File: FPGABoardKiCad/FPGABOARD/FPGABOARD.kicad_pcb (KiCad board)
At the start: 4 copper layers, 87 parts, among them J1 USB_C_Receptacle_USB2.0_14P, J2 12PMOD, J3 Conn_02x12_Odd_Even, J4 6PMOD, J5 I2C, SW1 ResetICE, SW2 BTN0, SW3 BTN1, SW4 BTN2, U1 ICE40HX1K-VQ100, U2 AP2127K-3.3, U3 W25Q32JVSS, U4 AP2127K-1.2, U5 FT2232HPQ, U6 93LCxxBxxOT, U7 IS62LV256AL, Y2 SG-210STF, Y3 SG-210STF

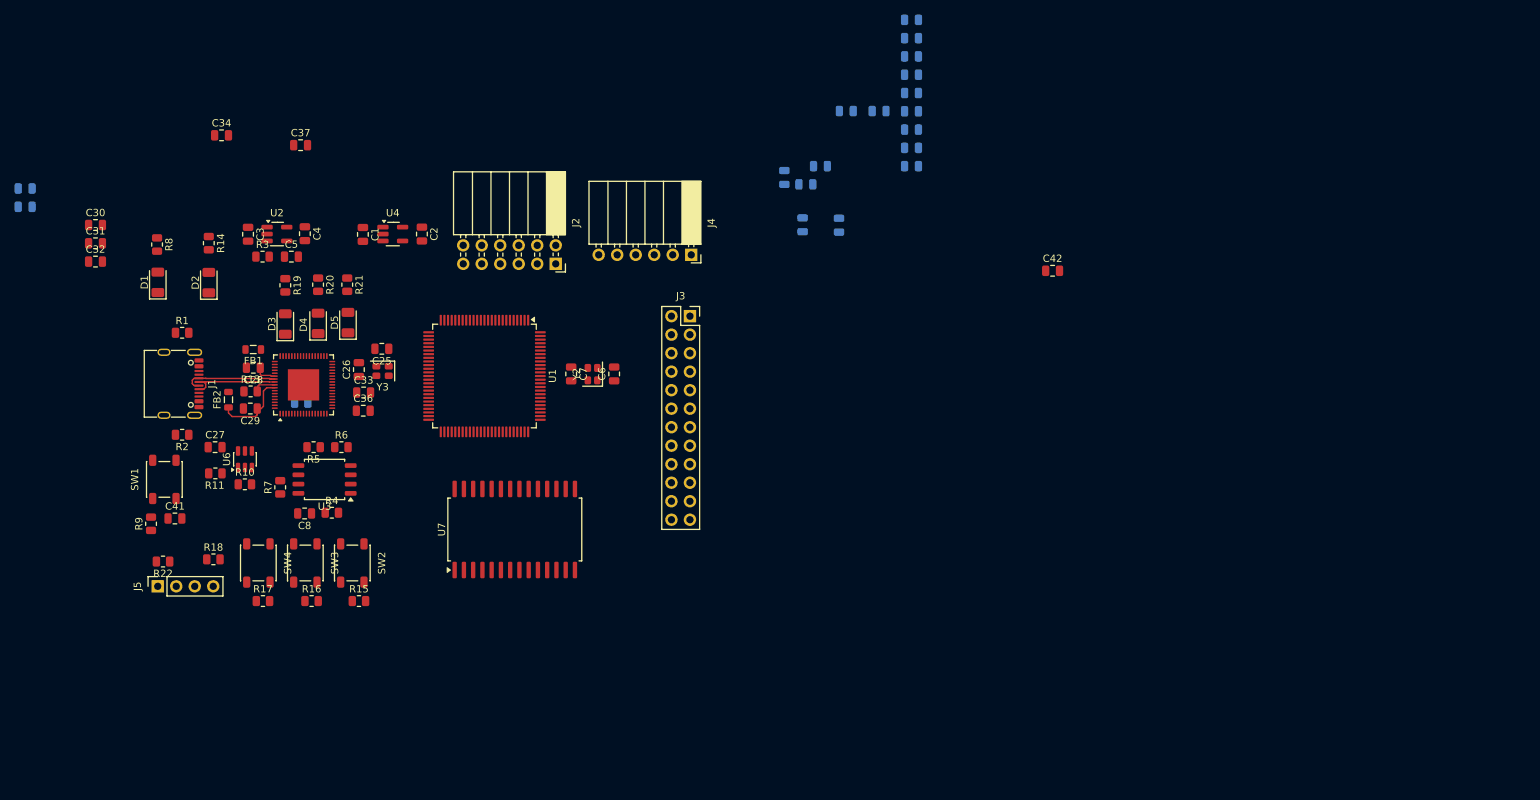
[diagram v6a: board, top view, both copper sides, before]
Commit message: Finsished up Header and Memory routing
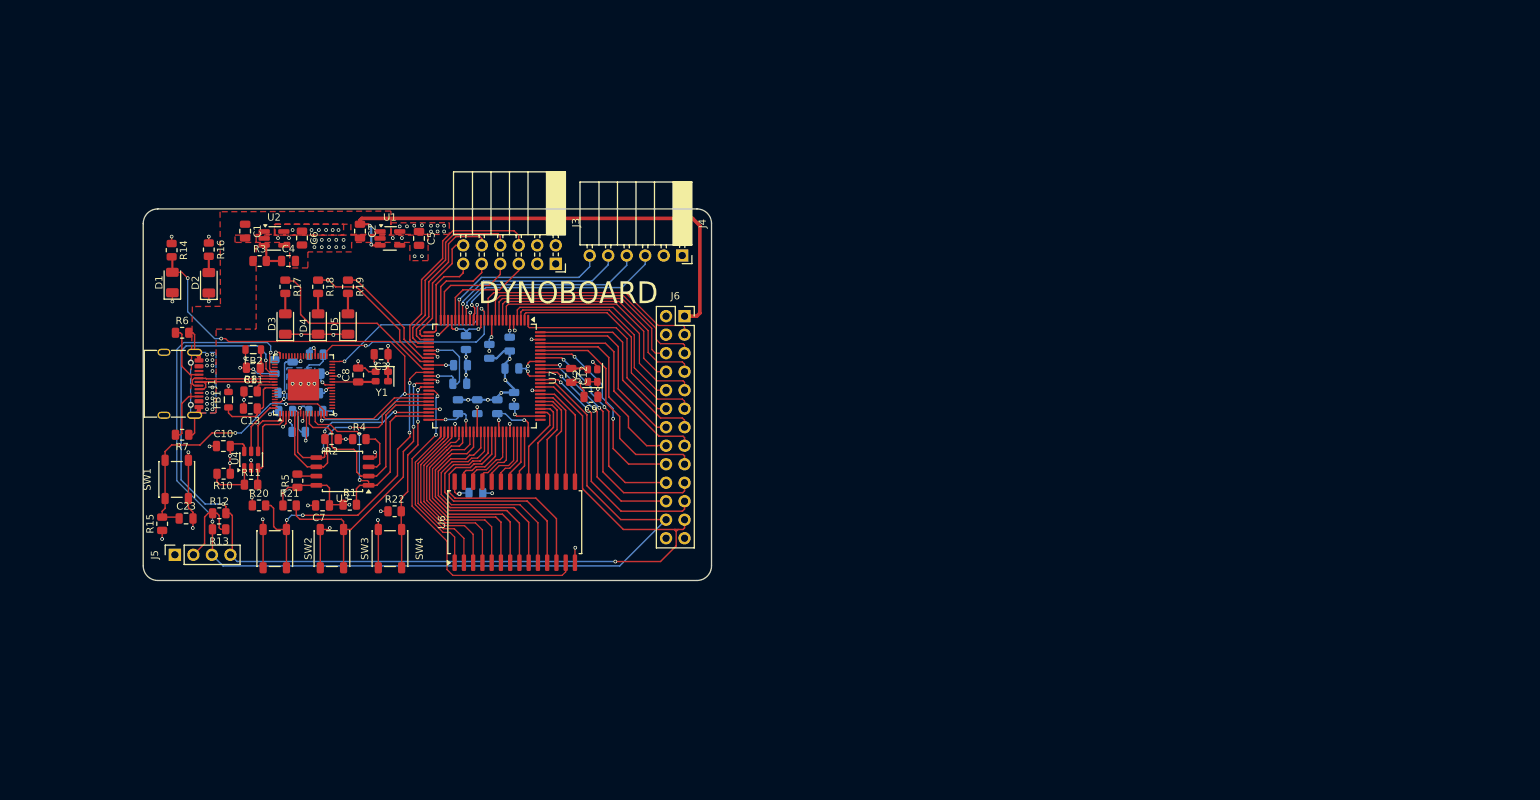
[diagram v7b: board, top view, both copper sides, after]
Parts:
- removed the C10 at (175.5, 78.2)
- removed the C11 at (170.5, 78.2)
- removed the C12 at (172.9, 70.1)
- removed the C13 at (170.9, 72.6)
- removed the C14 at (185.4, 50.0)
- removed the C20 at (185.4, 65.1)
- removed the C23 at (181.0, 62.6)
- removed C37, C38, C39, C42: 100n, Capacitor_SMD:C_0805_2012Metric
- removed the C9 at (168.0, 71.7)
- removed the J3 at (155.0, 90.7)
- added C25: 100n, Capacitor_SMD:C_0805_2012Metric, B.Cu at (123.5, 100.0)
- added C26: 100n, Capacitor_SMD:C_0805_2012Metric, B.Cu at (127.5, 95.5)
- added C27: 100n, Capacitor_SMD:C_0805_2012Metric, B.Cu at (128.6, 103.2)
- added C28: 100n, Capacitor_SMD:C_0805_2012Metric, B.Cu at (125.8, 103.2)
- added C29: 100n, Capacitor_SMD:C_0805_2012Metric, B.Cu at (123.2, 103.2)
- added J6: Conn_02x13_Odd_Even, Connector_PinSocket_2.54mm:PinSocket_2x13_P2.54mm_Vertical, F.Cu at (154.3, 90.7)
- C14: renamed from C36; moved to B.Cu
- C20: renamed from C33; moved to B.Cu
- C24: value 10u -> 100n
- C30, C31, C32, C34: moved to B.Cu
- moved C16 98.7 mm to (99.5, 103.8)
- moved C15 96.3 mm to (100.5, 98.0), turned to -90 degrees
- moved C18 95.2 mm to (98.0, 97.7), turned to -90 degrees
- moved C19 94.3 mm to (99.5, 101.2), turned to 0 degrees
- moved C17 93.9 mm to (103.7, 103.8), turned to 0 degrees
- moved C21 87.7 mm to (103.5, 98.6)
- moved C22 74.8 mm to (125.7, 115.0), turned to 0 degrees
- moved C24 63.4 mm to (123.5, 97.5), turned to 0 degrees
- moved C31 61.3 mm to (130.9, 102.2), turned to 90 degrees
- moved C32 59.0 mm to (130.6, 97.9), turned to 180 degrees
- moved C30 53.3 mm to (124.3, 94.3), turned to -90 degrees
- moved C34 48.8 mm to (130.3, 94.5), turned to -90 degrees
- moved R22 21.9 mm to (114.5, 117.5)
- moved R20 19.0 mm to (95.9, 116.7)
- moved SW4 18.2 mm to (113.9, 122.6)
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- renumbered C3 to C1, C27 to C10, C28 to C11, C7 to C12, C29 to C13, C1 to C2, C41 to C23, C25 to C3, C5 to C4, C2 to C5, C4 to C6, C8 to C7, C26 to C8, C6 to C9, FB2 to FB1, FB1 to FB2, J2 to J3, R4 to R1, R11 to R10, R10 to R11, R18 to R12, R22 to R13, R8 to R14, R9 to R15, R14 to R16, R19 to R17, R20 to R18, R21 to R19, R5 to R2, R15 to R20, R16 to R21, R17 to R22, R6 to R4, R7 to R5, R1 to R6, R2 to R7, R13 to R8, R12 to R9, U4 to U1, U6 to U4, U7 to U6, U1 to U7, Y3 to Y1
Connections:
- C15 pad 1: +3V3 -> +1V2
- C17 pad 1: +3V3 -> +1V2
- C19 pad 1: +3V3 -> +1V2
- C24 pad 1: +3V3 -> +1V2
- C31 pad 1: +3V3 -> +1V2
- U6 pad 1: unconnected-(U7-A14-Pad1) -> /RAMA14
- U6 pad 10: unconnected-(U7-A0-Pad10) -> /RAMA0
- U6 pad 11: unconnected-(U7-I/O0-Pad11) -> /RAMIO0
- U6 pad 12: unconnected-(U7-I/O1-Pad12) -> /RAMIO1
- U6 pad 13: unconnected-(U7-I/O2-Pad13) -> /RAMIO2
- U6 pad 15: unconnected-(U7-I/O3-Pad15) -> /RAMIO3
- U6 pad 16: unconnected-(U7-I/O4-Pad16) -> /RAMIO4
- U6 pad 17: unconnected-(U7-I/O5-Pad17) -> /RAMIO5
- U6 pad 18: unconnected-(U7-I/O6-Pad18) -> /RAMIO6
- U6 pad 19: unconnected-(U7-I/O7-Pad19) -> /RAMIO7
- U6 pad 2: unconnected-(U7-A12-Pad2) -> /RAMA12
- U6 pad 21: unconnected-(U7-A10-Pad21) -> /RAMA10
- U6 pad 23: unconnected-(U7-A11-Pad23) -> /RAMA11
- U6 pad 24: unconnected-(U7-A9-Pad24) -> /RAMA9
- U6 pad 25: unconnected-(U7-A8-Pad25) -> /RAMA8
- U6 pad 26: unconnected-(U7-A13-Pad26) -> /RAMA13
- U6 pad 3: unconnected-(U7-A7-Pad3) -> /RAMA7
- U6 pad 4: unconnected-(U7-A6-Pad4) -> /RAMA6
- U6 pad 5: unconnected-(U7-A5-Pad5) -> /RAMA5
- U6 pad 6: unconnected-(U7-A4-Pad6) -> /RAMA4
- U6 pad 7: unconnected-(U7-A3-Pad7) -> /RAMA3
- U6 pad 8: unconnected-(U7-A2-Pad8) -> /RAMA2
- U6 pad 9: unconnected-(U7-A1-Pad9) -> /RAMA1
- U7 pad 1: unconnected-(U1-IOL_1A-Pad1) -> /EXP13
- U7 pad 10: unconnected-(U1-IOL_5B-Pad10) -> /EXP1
- U7 pad 100: unconnected-(U1-IOT_95-Pad100) -> /EXP5
- U7 pad 12: unconnected-(U1-IOL_6A-Pad12) -> /EXP0
- U7 pad 13: unconnected-(U1-IOL_6B_GBIN7-Pad13) -> /ICETX
- U7 pad 15: unconnected-(U1-IOL_7A_GBIN6-Pad15) -> /ICERX
- U7 pad 16: unconnected-(U1-IOL_7B-Pad16) -> /PMOD3B
- U7 pad 18: unconnected-(U1-IOL_8A-Pad18) -> /PMOD2B
- U7 pad 19: unconnected-(U1-IOL_8B-Pad19) -> /PMOD1B
- U7 pad 2: unconnected-(U1-IOL_1B-Pad2) -> /EXP4
- U7 pad 20: unconnected-(U1-IOL_10A-Pad20) -> /PMOD0B
- U7 pad 21: unconnected-(U1-IOL_10B-Pad21) -> /PMOD7
- U7 pad 24: unconnected-(U1-IOL_12A-Pad24) -> /PMOD6
- U7 pad 25: unconnected-(U1-IOL_12B-Pad25) -> /PMOD5
- U7 pad 26: unconnected-(U1-IOB_26-Pad26) -> /PMOD4
- U7 pad 27: unconnected-(U1-IOB_27-Pad27) -> /PMOD0
- U7 pad 28: unconnected-(U1-IOB_28-Pad28) -> /PMOD1
- U7 pad 29: unconnected-(U1-IOB_29-Pad29) -> /PMOD2
- U7 pad 3: unconnected-(U1-IOL_2A-Pad3) -> /EXP12
- U7 pad 30: unconnected-(U1-IOB_30-Pad30) -> /PMOD3
- U7 pad 33: unconnected-(U1-IOB_35_GBIN5-Pad33) -> /LED2
- U7 pad 34: unconnected-(U1-IOB_36_GBIN4-Pad34) -> /LED1
- U7 pad 36: unconnected-(U1-IOB_34-Pad36) -> /LED0
- U7 pad 37: unconnected-(U1-IOB_37-Pad37) -> /BTN0
- U7 pad 4: unconnected-(U1-IOL_2B-Pad4) -> /EXP3
- U7 pad 40: unconnected-(U1-IOB_41-Pad40) -> /BTN1
- U7 pad 41: unconnected-(U1-IOB_42_CBSEL0-Pad41) -> /BTN2
- U7 pad 42: unconnected-(U1-IOB_43_CBSEL1-Pad42) -> /RAMIO2
- U7 pad 51: unconnected-(U1-IOR_52-Pad51) -> /RAMA14
- U7 pad 52: unconnected-(U1-IOR_53-Pad52) -> /RAMA12
- U7 pad 53: unconnected-(U1-IOR_54-Pad53) -> /RAMA7
- U7 pad 54: unconnected-(U1-IOR_55-Pad54) -> /RAMA6
- U7 pad 56: unconnected-(U1-IOR_56-Pad56) -> /RAMA5
- U7 pad 57: unconnected-(U1-IOR_57-Pad57) -> /RAMA4
- U7 pad 59: unconnected-(U1-IOR_58-Pad59) -> /RAMA3
- U7 pad 60: unconnected-(U1-IOR_59-Pad60) -> /RAMA2
- U7 pad 62: unconnected-(U1-IOR_60_GBIN3-Pad62) -> /RAMA1
- U7 pad 63: unconnected-(U1-IOR_61_GBIN2-Pad63) -> /RAMA0
- U7 pad 64: unconnected-(U1-IOR_63-Pad64) -> /RAMIO0
- U7 pad 65: unconnected-(U1-IOR_64-Pad65) -> /RAMIO1
- U7 pad 66: unconnected-(U1-IOR_65-Pad66) -> /RAM_WE
- U7 pad 68: unconnected-(U1-IOR_67-Pad68) -> /RAMA13
- U7 pad 69: unconnected-(U1-IOR_68-Pad69) -> /RAMA8
- U7 pad 7: unconnected-(U1-IOL_3A-Pad7) -> /EXP11
- U7 pad 71: unconnected-(U1-IOR_69-Pad71) -> /RAMA9
- U7 pad 72: unconnected-(U1-IOR_70-Pad72) -> /RAMA11
- U7 pad 73: unconnected-(U1-IOR_71-Pad73) -> /RAM_OE
- U7 pad 74: unconnected-(U1-IOR_72-Pad74) -> /RAMA10
- U7 pad 78: unconnected-(U1-IOT_73-Pad78) -> /RAM_CE
- U7 pad 79: unconnected-(U1-IOT_74-Pad79) -> /RAMIO7
- U7 pad 8: unconnected-(U1-IOL_3B-Pad8) -> /EXP2
- U7 pad 80: unconnected-(U1-IOT_75-Pad80) -> /RAMIO6
- U7 pad 81: unconnected-(U1-IOT_77-Pad81) -> /RAMIO5
- U7 pad 82: unconnected-(U1-IOT_78-Pad82) -> /RAMIO4
- U7 pad 83: unconnected-(U1-IOT_79-Pad83) -> /RAMIO3
- U7 pad 85: unconnected-(U1-IOT_80-Pad85) -> /SDA
- U7 pad 86: unconnected-(U1-IOT_81-Pad86) -> /SCL
- U7 pad 87: unconnected-(U1-IOT_82-Pad87) -> /EXP9
- U7 pad 89: unconnected-(U1-IOT_84_GBIN1-Pad89) -> /EXP18
- U7 pad 9: unconnected-(U1-IOL_5A-Pad9) -> /EXP10
- U7 pad 91: unconnected-(U1-IOT_86-Pad91) -> /EXP8
- U7 pad 93: unconnected-(U1-IOT_87-Pad93) -> /EXP17
- U7 pad 94: unconnected-(U1-IOT_88-Pad94) -> /EXP16
- U7 pad 95: unconnected-(U1-IOT_89-Pad95) -> /EXP7
- U7 pad 96: unconnected-(U1-IOT_90-Pad96) -> /EXP15
- U7 pad 97: unconnected-(U1-IOT_91-Pad97) -> /EXP6
- U7 pad 99: unconnected-(U1-IOT_93-Pad99) -> /EXP14
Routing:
- net /SDA: track 0.00 -> 149.1 mm, vias 0 -> 3
- net /SCL: track 0.00 -> 144.0 mm, vias 0 -> 2
- net GND: track 0.00 -> 126.3 mm, vias 0 -> 64
- net +3V3: track 0.00 -> 117.0 mm, vias 0 -> 38
- net +5V: track 0.00 -> 67.3 mm, vias 0 -> 18
- net /CDONE: track 0.00 -> 63.9 mm, vias 0 -> 4
- net /CRESET_B: track 0.00 -> 53.4 mm, vias 0 -> 2
- net /BTN0: track 0.00 -> 47.2 mm, vias 0 -> 4
- net /RAMIO2: track 0.00 -> 47.0 mm, vias 0 -> 2
- net /BTN1: track 0.00 -> 41.3 mm, vias 0 -> 2
- net /ICE_SS: track 0.00 -> 37.1 mm, vias 0 -> 2
- net /RAMIO1: track 0.00 -> 34.8 mm
- net /EXP9: track 0.00 -> 34.0 mm, vias 0 -> 2
- net /RAMIO0: track 0.00 -> 34.0 mm
- net /EXP1: track 0.00 -> 33.7 mm
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- added copper zone on F.Cu, net +1V2
- added copper zone on F.Cu, net +3V3
- added copper zone on In2.Cu, net +3V3
- added copper zone on B.Cu, net +5V
- added copper zone on F.Cu, net +5V
- added copper zone on B.Cu, net GND
- added copper zone on F.Cu, net GND
- added copper zone on In1.Cu, net GND
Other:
- board outline added: 78 x 51 mm
- board text added: "DYNOBOARD"

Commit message: Minor wiring change
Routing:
- net /LED1: track 20.7 -> 22.6 mm
- net /LED2: track 16.4 -> 18.0 mm
- net /RAMA9: track 8.83 -> 8.09 mm
- net /LED0: track 26.9 -> 27.4 mm
